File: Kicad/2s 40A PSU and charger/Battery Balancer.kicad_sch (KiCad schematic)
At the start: 20 parts, among them Q6 Vishay sir404dp, or SiR500DP, U1 BQ76905RGRR

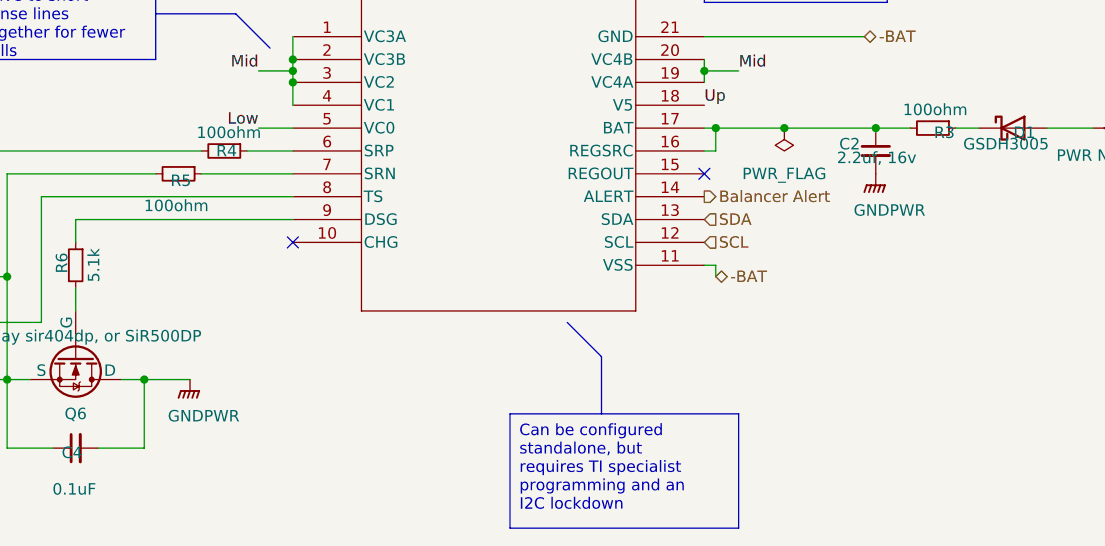
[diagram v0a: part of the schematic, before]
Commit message: Combined separate ground planes
I now have one solid ground plane. There really was no point in having separate ground planes EXCEPT for keeping the high current return path away from the MCU and sense lines. I have added a keepout zone on the top half, to split to keep the high current return from going into the MCU section, but that is it.
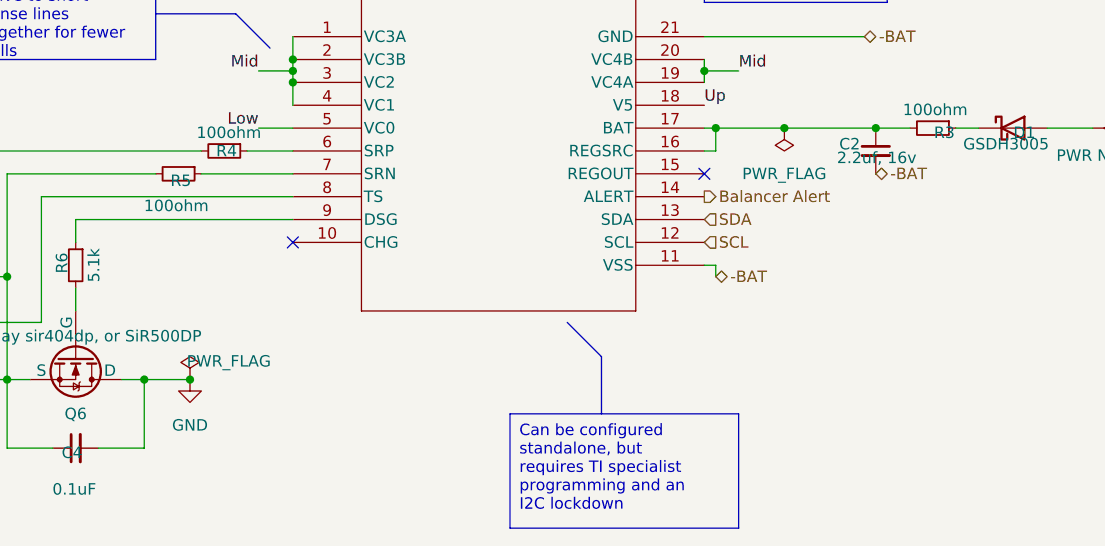
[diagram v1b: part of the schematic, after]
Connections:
- net -BAT: now also C2.2
- net GNDPWR renamed GND
- net GND: no longer C2.2
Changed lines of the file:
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@@
+	)
+	(junction
+		(at 90.17 113.03)
+		(diameter 0)
+		(color 0 0 0 0)
 	)
 	(junction
@@
 				)
 				(justify right)
+			)
+		)
+	)
+	(hierarchical_label "-BAT"
+		(shape bidirectional)
+		(at 166.37 90.17 0)
+		(fields_autoplaced yes)
+		(effects
+			(font
+				(size 1.27 1.27)
+			)
+			(justify left)
+		)
+		(property "Netclass" "High Current"
+			(at 166.37 91.44 0)
+			(effects
+				(font
+					(size 1.27 1.27)
+					(italic yes)
+				)
+				(justify left)
 			)
 		)
@@
 	)
 	(symbol
+		(lib_id "power:GND")
+		(at 90.17 113.03 0)
+		(unit 1)
+		(exclude_from_sim no)
+		(in_bom yes)
+		(on_board yes)
+		(dnp no)
+		(fields_autoplaced yes)
+		(property "Reference" "#PWR01"
+			(at 90.17 119.38 0)
+			(effects
+				(font
+					(size 1.27 1.27)
+				)
+				(hide yes)
+			)
+		)
+		(property "Value" "GND"
+			(at 90.17 118.11 0)
+			(effects
+				(font
+					(size 1.27 1.27)
+				)
+			)
+		)
+		(property "Footprint" ""
+			(at 90.17 113.03 0)
+			(effects
+				(font
+					(size 1.27 1.27)
+				)
+				(hide yes)
+			)
+		)
+		(property "Datasheet" ""
+			(at 90.17 113.03 0)
+			(effects
+				(font
+					(size 1.27 1.27)
+				)
+				(hide yes)
+			)
+		)
+		(property "Description" "Power symbol creates a global label with name \"GND\" , ground"
+			(at 90.17 113.03 0)
+			(effects
+				(font
+					(size 1.27 1.27)
+				)
+				(hide yes)
+			)
+		)
+		(pin "1"
+		)
+		(instances
+			(project "2s 40A PSU and charger"
+				(path "/eb3f183d-8bb1-43a5-a363-092ed67891e3/9cf42ac0-c980-41ef-957c-e7b7cc3eb205"
+					(reference "#PWR01")
+					(unit 1)
+				)
+			)
+		)
+	)
+	(symbol
 		(lib_id "Device:R_Small")
 		(at 77.47 100.33 0)
@@
 	)
 	(symbol
-		(lib_id "power:GNDPWR")
-		(at 90.17 113.03 0)
-		(unit 1)
-		(exclude_from_sim no)
-		(in_bom yes)
-		(on_board yes)
-		(dnp no)
-		(property "Reference" "#PWR01"
-			(at 90.17 118.11 0)
-			(effects
-				(font
-					(size 1.27 1.27)
-				)
-				(hide yes)
-			)
-		)
-		(property "Value" "GNDPWR"
-			(at 91.694 117.094 0)
-			(effects
-				(font
-					(size 1.27 1.27)
-				)
-			)
-		)
-		(property "Footprint" ""
-			(at 90.17 114.3 0)
-			(effects
-				(font
-					(size 1.27 1.27)
-				)
-				(hide yes)
-			)
-		)
-		(property "Datasheet" ""
-			(at 90.17 114.3 0)
-			(effects
-				(font
-					(size 1.27 1.27)
-				)
-				(hide yes)
-			)
-		)
-		(property "Description" "Power symbol creates a global label with name \"GNDPWR\" , global ground"
-			(at 90.17 113.03 0)
-			(effects
-				(font
-					(size 1.27 1.27)
-				)
-				(hide yes)
-			)
-		)
-		(pin "1"
-		)
-		(instances
-			(project "2s 40A PSU and charger"
-				(path "/eb3f183d-8bb1-43a5-a363-092ed67891e3/9cf42ac0-c980-41ef-957c-e7b7cc3eb205"
-					(reference "#PWR01")
-					(unit 1)
-				)
-			)
-		)
-	)
-	(symbol
 		(lib_id "Device:NetTie_2")
 		(at 229.87 91.44 180)
@@
 	)
 	(symbol
-		(lib_id "power:GNDPWR")
-		(at 166.37 90.17 0)
-		(unit 1)
-		(exclude_from_sim no)
-		(in_bom yes)
-		(on_board yes)
-		(dnp no)
-		(property "Reference" "#PWR03"
-			(at 166.37 95.25 0)
-			(effects
-				(font
-					(size 1.27 1.27)
-				)
-				(hide yes)
-			)
-		)
-		(property "Value" "GNDPWR"
-			(at 167.894 94.234 0)
-			(effects
-				(font
-					(size 1.27 1.27)
-				)
-			)
-		)
-		(property "Footprint" ""
-			(at 166.37 91.44 0)
-			(effects
-				(font
-					(size 1.27 1.27)
-				)
-				(hide yes)
-			)
-		)
-		(property "Datasheet" ""
-			(at 166.37 91.44 0)
-			(effects
-				(font
-					(size 1.27 1.27)
-				)
-				(hide yes)
-			)
-		)
-		(property "Description" "Power symbol creates a global label with name \"GNDPWR\" , global ground"
-			(at 166.37 90.17 0)
-			(effects
-				(font
-					(size 1.27 1.27)
-				)
-				(hide yes)
-			)
-		)
-		(pin "1"
-		)
-		(instances
-			(project "2s 40A PSU and charger"
-				(path "/eb3f183d-8bb1-43a5-a363-092ed67891e3/9cf42ac0-c980-41ef-957c-e7b7cc3eb205"
-					(reference "#PWR03")
-					(unit 1)
-				)
-			)
-		)
-	)
-	(symbol
 		(lib_id "Device:C_Small")
 		(at 166.37 87.63 0)
@@
 					(unit 1)
 				)
+			)
+		)
+	)
+	(symbol
+		(lib_id "power:PWR_FLAG")
+		(at 90.17 113.03 0)
+		(unit 1)
+		(exclude_from_sim no)
+		(in_bom yes)
+		(on_board yes)
+		(dnp no)
+		(property "Reference" "#FLG04"
+			(at 90.17 111.125 0)
+			(effects
+				(font
+					(size 1.27 1.27)
+				)
+				(hide yes)
+			)
+		)
+		(property "Value" "PWR_FLAG"
+			(at 94.488 110.998 0)
+			(effects
+				(font
+					(size 1.27 1.27)
+				)
+			)
+		)
+		(property "Footprint" ""
+			(at 90.17 113.03 0)
+			(effects
+				(font
+					(size 1.27 1.27)
+				)
+				(hide yes)
+			)
+		)
+		(property "Datasheet" "~"
+			(at 90.17 113.03 0)
+			(effects
+				(font
+					(size 1.27 1.27)
+				)
+				(hide yes)
+			)
+		)
+		(property "Description" "Special symbol for telling ERC where power comes from"
+			(at 90.17 113.03 0)
+			(effects
+				(font
+					(size 1.27 1.27)
+				)
+				(hide yes)
+			)
+		)
+		(pin "1"
+		)
+		(instances
+			(project "2s 40A PSU and charger"
+				(path "/eb3f183d-8bb1-43a5-a363-092ed67891e3/9cf42ac0-c980-41ef-957c-e7b7cc3eb205"
+					(reference "#FLG04")
+					(unit 1)
+				)

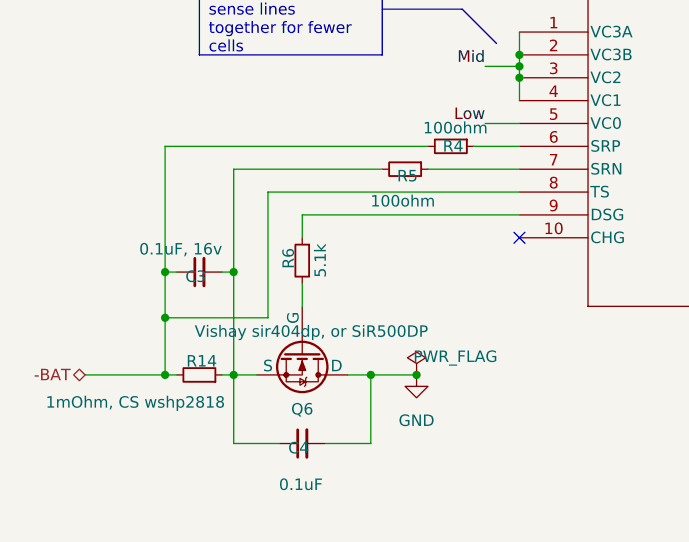
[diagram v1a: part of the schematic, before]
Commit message: Finished routing PSU
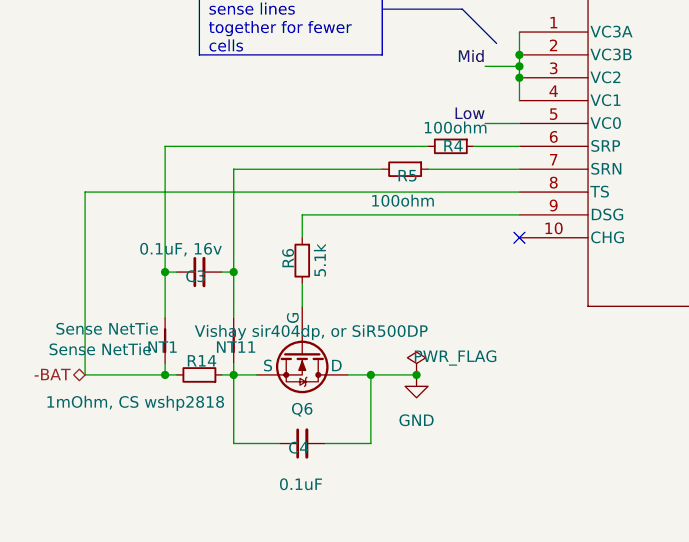
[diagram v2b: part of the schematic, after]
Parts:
- added NT1, NT11: Sense NetTie, custom_Connector:NetTie-2_SMD_Pad0.2mm, symbol Device:NetTie_2
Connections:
- net -BAT: now also NT1.1; no longer C3.1, R4.2
- net at C4.1, Q6.5 (S), R14.1: now also NT11.1; no longer C3.2, R5.2
- new net: C3.1, NT1.2, R4.2
- new net: C3.2, NT11.2, R5.2
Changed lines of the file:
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@@
-	)
-	(junction
-		(at 62.23 106.68)
-		(diameter 0)
-		(color 0 0 0 0)
 	)
 	(junction
@@
 	(wire
 		(pts
-			(xy 73.66 106.68) (xy 62.23 106.68)
-		)
-		(stroke
-			(width 0)
-			(type default)
-		)
-	)
-	(wire
-		(pts
-			(xy 73.66 92.71) (xy 73.66 106.68)
-		)
-		(stroke
-			(width 0)
-			(type default)
-		)
-	)
-	(wire
-		(pts
 			(xy 148.59 85.09) (xy 156.21 85.09)
 		)
@@
 	(wire
 		(pts
+			(xy 53.34 92.71) (xy 53.34 113.03)
+		)
+		(stroke
+			(width 0)
+			(type default)
+		)
+	)
+	(wire
+		(pts
 			(xy 223.52 85.09) (xy 237.49 85.09)
 		)
@@
 	(wire
 		(pts
+			(xy 53.34 92.71) (xy 101.6 92.71)
+		)
+		(stroke
+			(width 0)
+			(type default)
+		)
+	)
+	(wire
+		(pts
 			(xy 62.23 113.03) (xy 63.5 113.03)
 		)
@@
 	(wire
 		(pts
+			(xy 69.85 111.76) (xy 69.85 113.03)
+		)
+		(stroke
+			(width 0)
+			(type default)
+		)
+	)
+	(wire
+		(pts
 			(xy 77.47 102.87) (xy 77.47 105.41)
 		)
@@
 	(wire
 		(pts
-			(xy 62.23 106.68) (xy 62.23 113.03)
-		)
-		(stroke
-			(width 0)
-			(type default)
-		)
-	)
-	(wire
-		(pts
 			(xy 147.32 100.33) (xy 148.59 100.33)
 		)
@@
 		)
 	)
-	(wire
-		(pts
-			(xy 73.66 92.71) (xy 101.6 92.71)
-		)
-		(stroke
-			(width 0)
-			(type default)
-		)
-	)
 	(polyline
 		(pts
@@
 	(wire
 		(pts
-			(xy 69.85 101.6) (xy 69.85 113.03)
+			(xy 69.85 101.6) (xy 69.85 106.68)
 		)
 		(stroke
@@
 		(pts
 			(xy 147.32 77.47) (xy 147.32 78.74)
+		)
+		(stroke
+			(width 0)
+			(type default)
+		)
+	)
+	(wire
+		(pts
+			(xy 62.23 111.76) (xy 62.23 113.03)
 		)
 		(stroke
@@
 				)
 				(justify left)
+			)
+		)
+	)
+	(symbol
+		(lib_id "Device:NetTie_2")
+		(at 62.23 109.22 90)
+		(unit 1)
+		(exclude_from_sim no)
+		(in_bom no)
+		(on_board yes)
+		(dnp no)
+		(property "Reference" "NT1"
+			(at 60.198 109.982 90)
+			(effects
+				(font
+					(size 1.27 1.27)
+				)
+				(justify right)
+			)
+		)
+		(property "Value" "Sense NetTie"
+			(at 49.276 110.236 90)
+			(effects
+				(font
+					(size 1.27 1.27)
+				)
+				(justify right)
+			)
+		)
+		(property "Footprint" "custom_Connector:NetTie-2_SMD_Pad0.2mm"
+			(at 62.23 109.22 0)
+			(effects
+				(font
+					(size 1.27 1.27)
+				)
+				(hide yes)
+			)
+		)
+		(property "Datasheet" "~"
+			(at 62.23 109.22 0)
+			(effects
+				(font
+					(size 1.27 1.27)
+				)
+				(hide yes)
+			)
+		)
+		(property "Description" "Net tie, 2 pins"
+			(at 62.23 109.22 0)
+			(effects
+				(font
+					(size 1.27 1.27)
+				)
+				(hide yes)
+			)
+		)
+		(pin "1"
+		)
+		(pin "2"
+		)
+		(instances
+			(project "2s 40A PSU and charger"
+				(path "/eb3f183d-8bb1-43a5-a363-092ed67891e3/9cf42ac0-c980-41ef-957c-e7b7cc3eb205"
+					(reference "NT1")
+					(unit 1)
+				)
 			)
 		)
@@
 					(unit 1)
 				)
+			)
+		)
+	)
+	(symbol
+		(lib_id "Device:NetTie_2")
+		(at 69.85 109.22 90)
+		(unit 1)
+		(exclude_from_sim no)
+		(in_bom no)
+		(on_board yes)
+		(dnp no)
+		(property "Reference" "NT11"
+			(at 67.818 109.982 90)
+			(effects
+				(font
+					(size 1.27 1.27)
+				)
+				(justify right)
+			)
+		)
+		(property "Value" "Sense NetTie"
+			(at 50.038 107.95 90)
+			(effects
+				(font
+					(size 1.27 1.27)
+				)
+				(justify right)
+			)
+		)
+		(property "Footprint" "custom_Connector:NetTie-2_SMD_Pad0.2mm"
+			(at 69.85 109.22 0)
+			(effects
+				(font
+					(size 1.27 1.27)
+				)
+				(hide yes)
+			)
+		)
+		(property "Datasheet" "~"
+			(at 69.85 109.22 0)
+			(effects
+				(font
+					(size 1.27 1.27)
+				)
+				(hide yes)
+			)
+		)
+		(property "Description" "Net tie, 2 pins"
+			(at 69.85 109.22 0)
+			(effects
+				(font
+					(size 1.27 1.27)
+				)
+				(hide yes)
+			)
+		)
+		(pin "1"
+		)
+		(pin "2"
+		)
+		(instances
+			(project "2s 40A PSU and charger"
+				(path "/eb3f183d-8bb1-43a5-a363-092ed67891e3/9cf42ac0-c980-41ef-957c-e7b7cc3eb205"
+					(reference "NT11")
+					(unit 1)
+				)

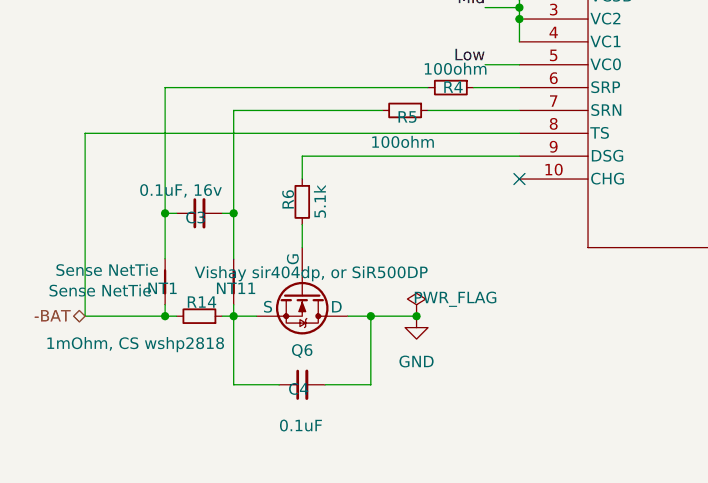
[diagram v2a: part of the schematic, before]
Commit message: Fixed incorrect mosfet pin assignments
This was an issue from the last test board I designed that I didn't catch. The mosfets have different pin assignments for drain, gate, and source, and I had messed those up in the schematic by choosing the wrong symbol. This should be fixed now
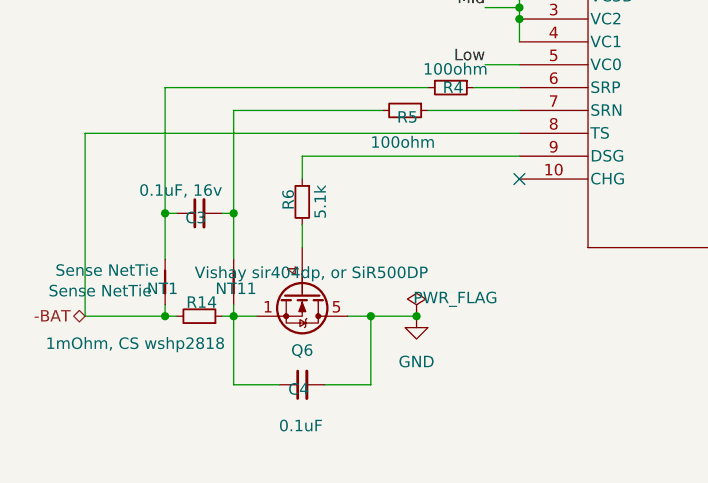
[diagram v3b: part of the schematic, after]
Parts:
- Q6: symbol Simulation_SPICE:NMOS -> custom_Device:Q_NMOS_SGD_8-pin
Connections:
- net GND: now also Q6.5 (D), Q6.6 (D), Q6.7 (D), Q6.8 (D); no longer Q6.1 (D), Q6.2 (D), Q6.3 (D)
- net at C4.1, NT11.1, R14.1: now also Q6.1 (S), Q6.2 (S), Q6.3 (S); no longer Q6.5 (S)
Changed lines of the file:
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@@
 	)
 	(symbol
-		(lib_name "NMOS_1")
-		(lib_id "Simulation_SPICE:NMOS")
+		(lib_id "custom_Device:Q_NMOS_SGD_8-pin")
 		(at 77.47 110.49 270)
 		(unit 1)
@@
 			)
 		)
-		(property "Datasheet" "https://ngspice.sourceforge.io/docs/ngspice-html-manual/manual.xhtml#cha_MOSFETs"
-			(at 64.77 110.49 0)
+		(property "Datasheet" "~"
+			(at 77.47 110.49 0)
 			(effects
 				(font
@@
 			)
 		)
-		(property "Description" "N-MOSFET transistor, drain/source/gate"
+		(property "Description" "N-MOSFET transistor, source/gate/drain"
 			(at 77.47 110.49 0)
 			(effects
@@
 			)
 		)
-		(property "Sim.Pins" "1=D 2=G 3=S"
+		(property "Sim.Pins" "1,2,3=S 4=G 5,6,7,8=D"
 			(at 62.23 110.49 0)
 			(effects
@@
 		(pin "1"
 		)
+		(pin "2"
+		)
+		(pin "3"
+		)
 		(pin "4"
 		)
 		(pin "5"
 		)
-		(pin "2"
+		(pin "7"
 		)
-		(pin "3"
+		(pin "8"
+		)
+		(pin "6"
 		)
 		(instances

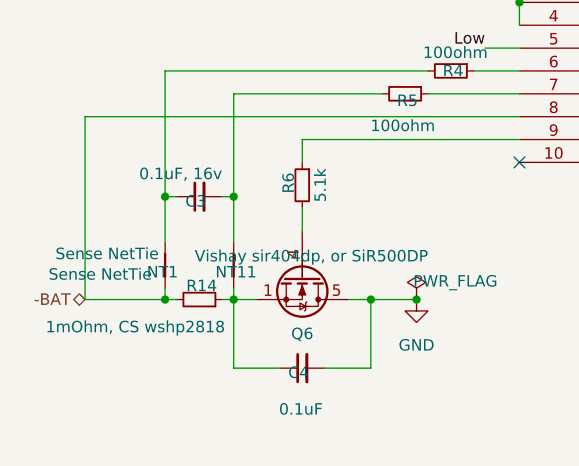
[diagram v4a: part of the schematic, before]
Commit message: Added LCSC part numbers, DNP attr, and exported Gerbers
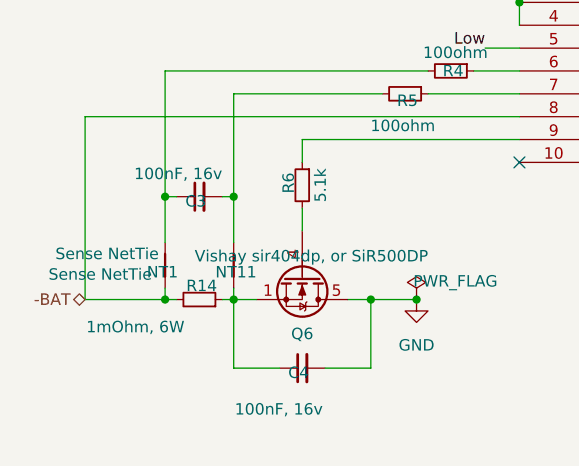
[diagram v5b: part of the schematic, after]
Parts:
- C13, C18, C19: LCSC (none) -> C16772
- C2: LCSC (none) -> C23630
- C3: value 0.1uF, 16v -> 100nF, 16v; LCSC (none) -> C1525
- C4: value 0.1uF -> 100nF, 16v; LCSC (none) -> C1525
- D1: LCSC (none) -> C2837790
- Q6: LCSC (none) -> C3289487
- R14: value 1mOhm, CS wshp2818 -> 1mOhm, 6W; footprint Resistor_SMD:R_2816_7142Metric -> Resistor_SMD:R_2512_6332Metric; LCSC (none) -> C19270875
- R15, R16, R17: LCSC (none) -> C25077
- R3, R4, R5: LCSC (none) -> C25076
- R6: LCSC (none) -> C25905
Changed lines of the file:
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@@
 			)
 		)
-		(property "Value" "0.1uF, 16v"
+		(property "Value" "100nF, 16v"
 			(at 68.58 99.06 90)
 			(effects
@@
 		(property "Description" "Unpolarized capacitor, small symbol"
 			(at 66.04 101.6 0)
+			(effects
+				(font
+					(size 1.27 1.27)
+				)
+				(hide yes)
+			)
+		)
+		(property "LCSC" "C1525"
+			(at 66.802 102.108 0)
 			(effects
 				(font
@@
 			)
 		)
+		(property "LCSC" "C25905"
+			(at 75.946 100.076 0)
+			(effects
+				(font
+					(size 1.27 1.27)
+				)
+				(hide yes)
+			)
+		)
 		(pin "2"
 		)
@@
 			)
 		)
+		(property "LCSC" "C25076"
+			(at 173.99 85.598 0)
+			(effects
+				(font
+					(size 1.27 1.27)
+				)
+				(hide yes)
+			)
+		)
 		(pin "2"
 		)
@@
 		(property "Sim.Pins" "1,2,3=S 4=G 5,6,7,8=D"
 			(at 62.23 110.49 0)
+			(effects
+				(font
+					(size 1.27 1.27)
+				)
+				(hide yes)
+			)
+		)
+		(property "LCSC" "C3289487"
+			(at 77.47 116.84 0)
 			(effects
 				(font
@@
 			)
 		)
-		(property "Value" "0.1uF"
+		(property "Value" "100nF, 16v"
 			(at 79.756 125.222 90)
 			(effects
@@
 		(property "Description" "Unpolarized capacitor, small symbol"
 			(at 77.47 120.65 0)
+			(effects
+				(font
+					(size 1.27 1.27)
+				)
+				(hide yes)
+			)
+		)
+		(property "LCSC" "C1525"
+			(at 78.232 121.158 0)
 			(effects
 				(font
@@
 			)
 		)
+		(property "LCSC" "C25077"
+			(at 239.522 83.312 0)
+			(effects
+				(font
+					(size 1.27 1.27)
+				)
+				(hide yes)
+			)
+		)
 		(pin "2"
 		)
@@
 			)
 		)
+		(property "LCSC" "C16772"
+			(at 253.492 94.742 0)
+			(effects
+				(font
+					(size 1.27 1.27)
+				)
+				(hide yes)
+			)
+		)
 		(pin "1"
 		)
@@
 			)
 		)
+		(property "LCSC" "C16772"
+			(at 250.952 88.392 0)
+			(effects
+				(font
+					(size 1.27 1.27)
+				)
+				(hide yes)
+			)
+		)
 		(pin "1"
 		)
@@
 			)
 		)
+		(property "LCSC" "C2837790"
+			(at 182.88 85.598 0)
+			(effects
+				(font
+					(size 1.27 1.27)
+				)
+				(hide yes)
+			)
+		)
 		(pin "2"
 		)
@@
 		(property "Description" "Resistor, small symbol"
 			(at 93.98 87.63 0)
+			(effects
+				(font
+					(size 1.27 1.27)
+				)
+				(hide yes)
+			)
+		)
+		(property "LCSC" "C25076"
+			(at 94.234 87.63 0)
 			(effects
 				(font
@@
 			)
 		)
-		(property "Value" "1mOhm, CS wshp2818"
+		(property "Value" "1mOhm, 6W"
 			(at 58.928 116.078 90)
 			(effects
@@
 			)
 		)
-		(property "Footprint" "Resistor_SMD:R_2816_7142Metric"
+		(property "Footprint" "Resistor_SMD:R_2512_6332Metric"
 			(at 66.04 113.03 0)
 			(effects
@@
 			)
 		)
+		(property "LCSC" "C19270875"
+			(at 66.04 113.03 90)
+			(effects
+				(font
+					(size 1.27 1.27)
+				)
+				(hide yes)
+			)
+		)
 		(pin "2"
 		)
@@
 			)
 		)
+		(property "LCSC" "C25076"
+			(at 89.154 90.932 0)
+			(effects
+				(font
+					(size 1.27 1.27)
+				)
+				(hide yes)
+			)
+		)
 		(pin "2"
 		)
@@
 			)
 		)
+		(property "LCSC" "C25077"
+			(at 245.872 89.662 0)
+			(effects
+				(font
+					(size 1.27 1.27)
+				)
+				(hide yes)
+			)
+		)
 		(pin "2"
 		)
@@
 		(property "Description" "Unpolarized capacitor, small symbol"
 			(at 166.37 87.63 0)
+			(effects
+				(font
+					(size 1.27 1.27)
+				)
+				(hide yes)
+			)
+		)
+		(property "LCSC" "C23630"
+			(at 162.306 86.868 0)
 			(effects
 				(font
@@
 			)
 		)
+		(property "LCSC" "C16772"
+			(at 253.492 83.312 0)
+			(effects
+				(font
+					(size 1.27 1.27)
+				)
+				(hide yes)
+			)
+		)
 		(pin "1"
 		)
@@
 			(effects
 				(font
+					(size 1.27 1.27)
+				)
+				(hide yes)
+			)
+		)
+		(property "LCSC" "C25077"
+			(at 245.872 78.232 0)
+			(effects
+				(font

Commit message: Fixed Current sense resistor footprints, adjusted current GND blocks
I had to source alternative resistors and change the footprints as well. I didn't realize though that the 2818 footprint I had was wrong though, 2816 is not quite compatible!

Another thing I did was fix gnd guides and added horse shoe shapes around the sensitive component vias.
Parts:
- R14: footprint Resistor_SMD:R_2512_6332Metric -> custom_Passives:R_2512_6332Metric_6W
- U1: LCSC (none) -> C22394458
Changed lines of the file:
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@@
+			)
+		)
+		(property "LCSC" "C22394458"
+			(at 124.46 64.77 0)
+			(effects
+				(font
+					(size 1.27 1.27)
+				)
+				(hide yes)
 			)
 		)
@@
 			)
 		)
-		(property "Footprint" "Resistor_SMD:R_2512_6332Metric"
+		(property "Footprint" "custom_Passives:R_2512_6332Metric_6W"
 			(at 66.04 113.03 0)
 			(effects
